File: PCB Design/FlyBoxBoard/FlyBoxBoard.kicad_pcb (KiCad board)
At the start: 2 copper layers, 148.6 x 119.4 mm, 42 parts, among them J1 5V in, J10 RED, J11 GREEN, J12 WHITE, J13 INFRARED, J14 LCD, J15 SD card reader, J16 5K Ohms, J17 5K Ohms, J18 ESP 32 Left Side extra pins, J19 ESP 32 Left Side extra pinouts, J2 12V in, J20 Transistor, J21 Logic Level LV pinouts, J22 Potentiometer, J23 Logic Level Left Side LV, J24 ESP 32 Right Side extra pinou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, J25 ESP 32 Right Side extra pinou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, J26 BuckPuck IR, J27 Logic Level Right Side HV, J28 Logic Level HV pins, J29 5K Ohms, J3 ESP 32 Left Side, J30 5K Ohms, J31 5K Ohms, J32 5K Ohms, J33 5K Ohms, J34 5K Ohms, J35 Transistor, J36 Transistor, J37 Transistor, J38 BuckPuck White, J39 BuckPuck Green, J4 Real Time Controller, J40 BuckPuck Red, J5 ESP 32 Right Side, J9 FAN

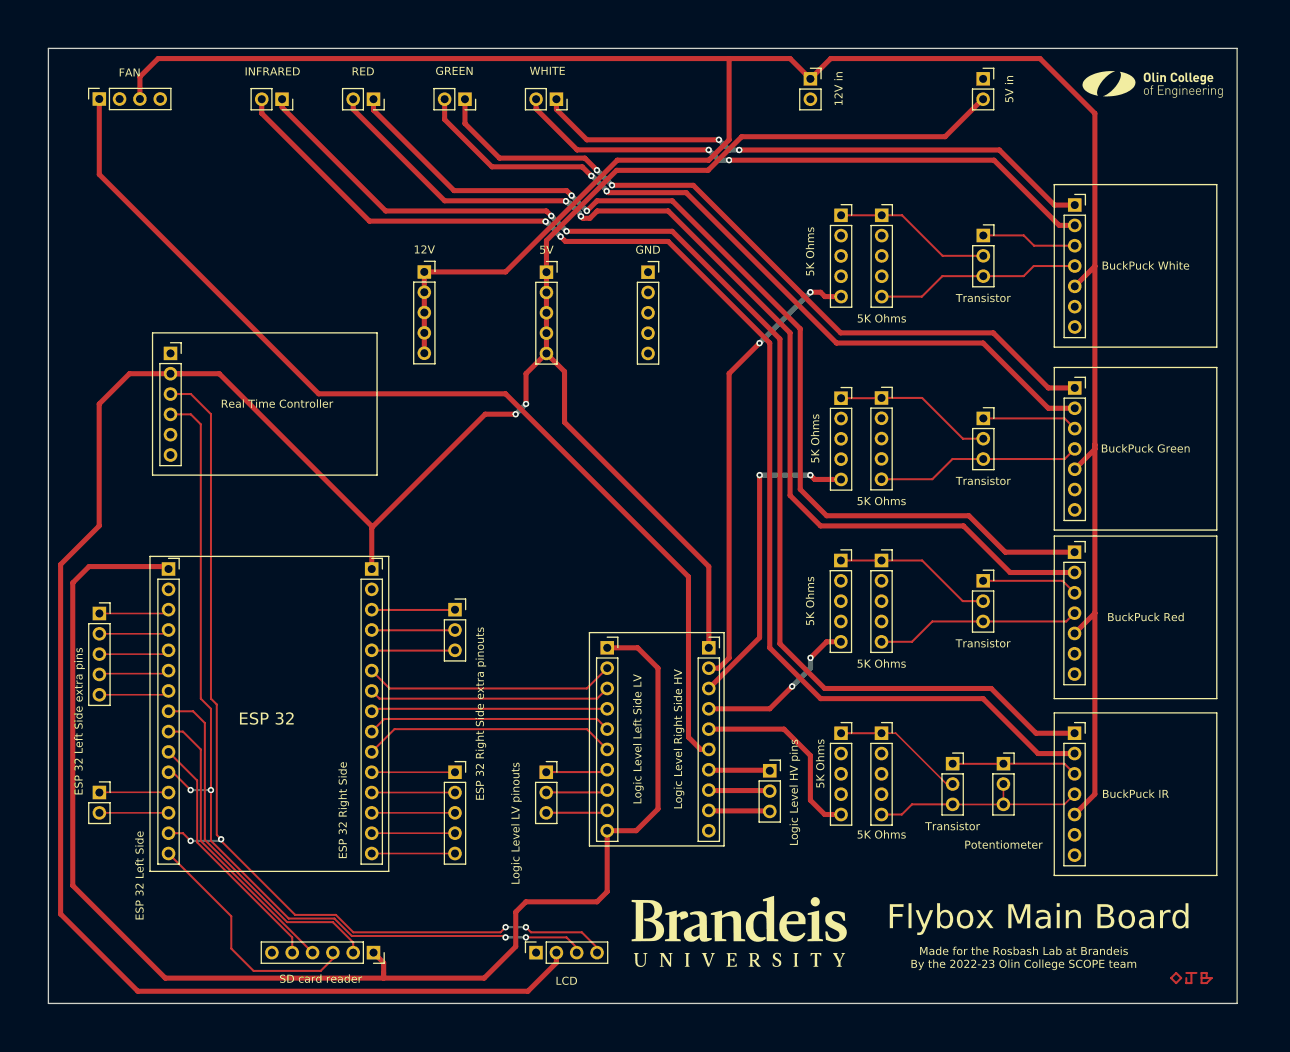
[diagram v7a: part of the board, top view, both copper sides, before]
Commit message: Updated mounting holes and rounded corneres
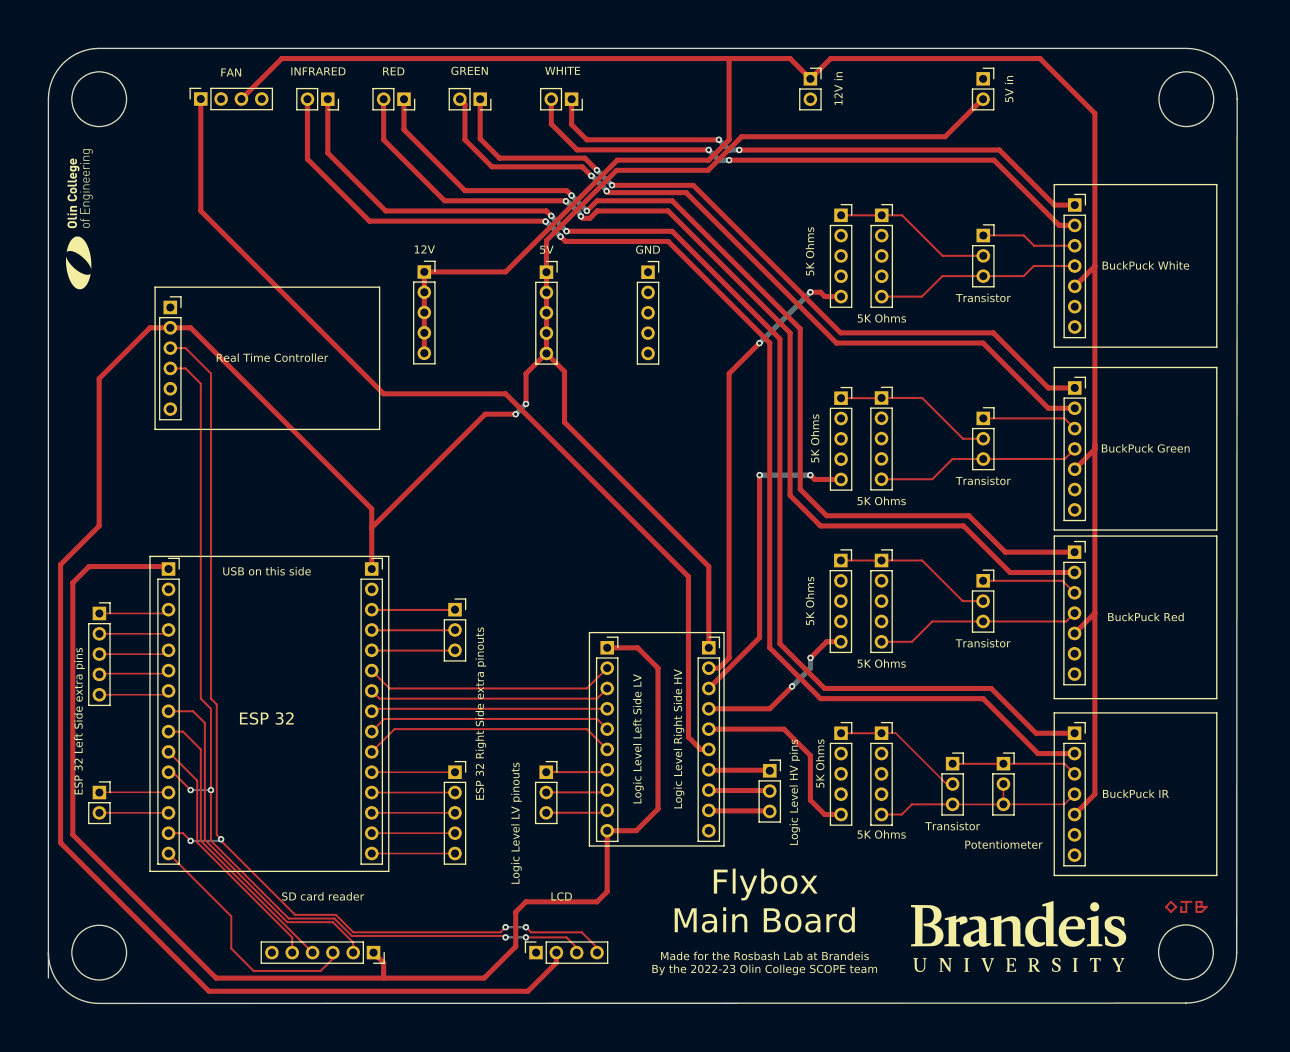
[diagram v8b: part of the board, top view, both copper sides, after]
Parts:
- moved G*** 135.1 mm to (20.3, 38.1), turned to 90 degrees
- moved G*** 34.9 mm to (137.8, 127.6)
- moved J9 12.7 mm to (35.6, 22.8)
- moved J4 5.74 mm to (31.8, 48.9)
- moved J13 5.72 mm to (51.4, 22.9)
- moved J10 3.81 mm to (61.0, 22.9)
- moved J11 1.91 mm to (70.5, 22.9)
- moved J12 1.91 mm to (81.9, 22.9)
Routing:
- net /12V: track 293.2 -> 278.9 mm
- net /HV5: track 127.1 -> 117.1 mm
- net /D21: track 115.0 -> 120.4 mm
- net /D22: track 120.7 -> 126.1 mm
- net /3V3: track 173.2 -> 169.5 mm
- net /R LED+: track 124.7 -> 122.3 mm
- net /IR LED-: track 158.9 -> 156.6 mm
- net /IR LED+: track 154.8 -> 152.4 mm
- net /R LED-: track 128.2 -> 126.6 mm
- net /5V: track 338.9 -> 340.3 mm
- net /W LED-: track 74.6 -> 73.8 mm
- net /G LED+: track 93.0 -> 92.2 mm
- net /W LED+: track 71.0 -> 70.2 mm
- net /G LED-: track 96.4 -> 95.6 mm
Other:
- outline, holes or cut-outs redrawn
- board text added: "USB on this side"
